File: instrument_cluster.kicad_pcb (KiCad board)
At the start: 2 copper layers, 146 x 45.7 mm, 76 parts, among them J1 Conn_02x16_Top_Bottom, J2 Conn_02x16_Top_Bottom, J3 USB mini-B SMD, J4 NOT_FITTED_SWD_Conn_01x04_Male, J5 54819-0572, J6 NOT_FITTED_SWD_Conn_01x04_Male, U1 LM2575S-5.0_NOPB, U10 74HC4050D, U11 TJA1040T, U12 TJA1040T, U2 LM2575S-5.0_NOPB, U3 LD1117S33TR_SOT223, U4 LD1117S33TR_SOT223, U5 STM32F105RBTx, U6 TJA1040T, U7 TJA1040T, U8 74HC4050D, U9 STM32F105RBTx, Y1 Crystal KX-13 25MHz, Y2 Crystal KX-13 25MHz

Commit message: rescue the stm32 mcu_s, add pcb list info
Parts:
- moved U5 93.4 mm to (149.9, 140.9)
- moved U9 93.1 mm to (134.0, 140.9)
- moved J5 86.7 mm to (106.4, 130.2), turned to 90 degrees
- moved J3 77.6 mm to (98.5, 85.7), turned to 270 degrees
- moved J2 69.4 mm to (69.8, 88.9)
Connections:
- J1 pad 10: Net-(J1-Pad10) -> (no net)
- J1 pad 11: Net-(J1-Pad11) -> (no net)
- J1 pad 14: Net-(J1-Pad14) -> (no net)
- J1 pad 20: /RR_FOG -> (no net)
- J1 pad 23: Net-(J1-Pad23) -> (no net)
- J1 pad 24: /FR_FOG -> (no net)
- J1 pad 25: Net-(J1-Pad25) -> (no net)
- J1 pad 26: Net-(J1-Pad26) -> (no net)
- J1 pad 28: Net-(J1-Pad28) -> (no net)
- J1 pad 29: Net-(J1-Pad29) -> (no net)
- J1 pad 30: Net-(J1-Pad30) -> (no net)
- J2 pad 10: Net-(J2-Pad10) -> (no net)
- J2 pad 11: Net-(J2-Pad11) -> (no net)
- J2 pad 13: Net-(J2-Pad13) -> (no net)
- J2 pad 14: Net-(J2-Pad14) -> (no net)
- J2 pad 16: Net-(J2-Pad16) -> (no net)
- J2 pad 17: Net-(J2-Pad17) -> (no net)
- J2 pad 18: Net-(J2-Pad18) -> (no net)
- J2 pad 19: Net-(J2-Pad19) -> (no net)
- J2 pad 2: Net-(J2-Pad2) -> (no net)
- J2 pad 20: Net-(J2-Pad20) -> (no net)
- J2 pad 22: Net-(J2-Pad22) -> (no net)
- J2 pad 24: Net-(J2-Pad24) -> (no net)
- J2 pad 25: Net-(J2-Pad25) -> (no net)
- J2 pad 26: Net-(J2-Pad26) -> (no net)
- J2 pad 27: Net-(J2-Pad27) -> (no net)
- J2 pad 28: /LIN_(contact_spiral) -> (no net)
- J2 pad 29: Net-(J2-Pad29) -> (no net)
- J2 pad 3: Net-(J2-Pad3) -> (no net)
- J2 pad 30: Net-(J2-Pad30) -> (no net)
- J2 pad 31: /ESCL -> (no net)
- J2 pad 32: Net-(J2-Pad32) -> (no net)
- J2 pad 4: Net-(J2-Pad4) -> (no net)
- J2 pad 6: Net-(J2-Pad6) -> (no net)
- J2 pad 8: Net-(J2-Pad8) -> (no net)
- J3 pad 4: Net-(J3-Pad4) -> (no net)
- J5 pad 4: Net-(J5-Pad4) -> (no net)
- U10 pad 13: Net-(U10-Pad13) -> (no net)
- U10 pad 14: Net-(U10-Pad14) -> (no net)
- U10 pad 15: Net-(U10-Pad15) -> (no net)
- U10 pad 16: Net-(U10-Pad16) -> (no net)
- U5 pad 10: Net-(U5-Pad10) -> (no net)
- U5 pad 11: Net-(U5-Pad11) -> (no net)
- U5 pad 14: Net-(U5-Pad14) -> (no net)
- U5 pad 15: Net-(U5-Pad15) -> (no net)
- U5 pad 16: Net-(U5-Pad16) -> (no net)
- U5 pad 17: Net-(U5-Pad17) -> (no net)
- U5 pad 2: Net-(U5-Pad2) -> (no net)
- U5 pad 20: Net-(U5-Pad20) -> (no net)
- U5 pad 21: Net-(U5-Pad21) -> (no net)
- U5 pad 22: Net-(U5-Pad22) -> (no net)
- U5 pad 23: Net-(U5-Pad23) -> (no net)
- U5 pad 24: Net-(U5-Pad24) -> (no net)
- U5 pad 25: Net-(U5-Pad25) -> (no net)
- U5 pad 26: Net-(U5-Pad26) -> (no net)
- U5 pad 27: Net-(U5-Pad27) -> (no net)
- U5 pad 28: Net-(U5-Pad28) -> (no net)
- U5 pad 29: Net-(U5-Pad29) -> (no net)
- U5 pad 3: Net-(U5-Pad3) -> (no net)
- U5 pad 30: Net-(U5-Pad30) -> (no net)
- U5 pad 33: Net-(U5-Pad33) -> (no net)
- U5 pad 34: Net-(U5-Pad34) -> (no net)
- U5 pad 35: Net-(U5-Pad35) -> (no net)
- U5 pad 36: Net-(U5-Pad36) -> (no net)
- U5 pad 37: Net-(U5-Pad37) -> (no net)
- U5 pad 38: Net-(U5-Pad38) -> (no net)
- U5 pad 39: Net-(U5-Pad39) -> (no net)
- U5 pad 4: Net-(U5-Pad4) -> (no net)
- U5 pad 40: Net-(U5-Pad40) -> (no net)
- U5 pad 41: Net-(U5-Pad41) -> (no net)
- U5 pad 43: Net-(U5-Pad43) -> (no net)
- U5 pad 50: Net-(U5-Pad50) -> (no net)
- U5 pad 51: Net-(U5-Pad51) -> (no net)
- U5 pad 52: Net-(U5-Pad52) -> (no net)
- U5 pad 53: Net-(U5-Pad53) -> (no net)
- U5 pad 54: Net-(U5-Pad54) -> (no net)
- U5 pad 55: Net-(U5-Pad55) -> (no net)
- U5 pad 56: Net-(U5-Pad56) -> (no net)
- U5 pad 59: Net-(U5-Pad59) -> (no net)
- U5 pad 60: Net-(U5-Pad60) -> (no net)
- U5 pad 7: Net-(U5-Pad7) -> (no net)
- U5 pad 8: Net-(U5-Pad8) -> (no net)
- U5 pad 9: Net-(U5-Pad9) -> (no net)
- U8 pad 13: Net-(U8-Pad13) -> (no net)
- U8 pad 14: Net-(U8-Pad14) -> (no net)
- U8 pad 15: Net-(U8-Pad15) -> (no net)
- U8 pad 16: Net-(U8-Pad16) -> (no net)
- U9 pad 10: Net-(U9-Pad10) -> (no net)
- U9 pad 14: Net-(U9-Pad14) -> (no net)
- U9 pad 16: Net-(U9-Pad16) -> (no net)
- U9 pad 2: Net-(U9-Pad2) -> (no net)
- U9 pad 20: Net-(U9-Pad20) -> (no net)
- U9 pad 25: Net-(U9-Pad25) -> (no net)
- U9 pad 26: Net-(U9-Pad26) -> (no net)
- U9 pad 27: Net-(U9-Pad27) -> (no net)
- U9 pad 28: Net-(U9-Pad28) -> (no net)
- U9 pad 29: /Module B (2can_filter+extra)/LIN_TXD -> (no net)
- U9 pad 3: Net-(U9-Pad3) -> (no net)
- U9 pad 30: /Module B (2can_filter+extra)/LIN_RXD -> (no net)
- U9 pad 33: /Module B (2can_filter+extra)/LIN_SLP -> (no net)
- U9 pad 34: Net-(U9-Pad34) -> (no net)
- U9 pad 35: Net-(U9-Pad35) -> (no net)
- U9 pad 36: Net-(U9-Pad36) -> (no net)
- U9 pad 4: Net-(U9-Pad4) -> (no net)
- U9 pad 41: Net-(U9-Pad41) -> (no net)
- U9 pad 43: Net-(U9-Pad43) -> (no net)
- U9 pad 50: Net-(U9-Pad50) -> (no net)
- U9 pad 51: Net-(U9-Pad51) -> (no net)
- U9 pad 53: Net-(U9-Pad53) -> (no net)
- U9 pad 54: Net-(U9-Pad54) -> (no net)
- U9 pad 55: Net-(U9-Pad55) -> (no net)
- U9 pad 56: Net-(U9-Pad56) -> (no net)
- U9 pad 59: Net-(U9-Pad59) -> (no net)
- U9 pad 60: Net-(U9-Pad60) -> (no net)
- U9 pad 7: Net-(U9-Pad7) -> (no net)
- U9 pad 8: Net-(U9-Pad8) -> (no net)
- U9 pad 9: Net-(U9-Pad9) -> (no net)

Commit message: pcb part replace
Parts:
- U2: footprint zulljon:TO170P1435X457-6N -> TO_SOT_Packages_SMD:TO-263-5_TabPin6
- U5, U9: moved to B.Cu
- moved D2 93.2 mm to (191.5, 126.0), turned to 270 degrees
- moved C2 89.3 mm to (186.0, 124.8), turned to 270 degrees
- moved U2 80.3 mm to (173.8, 121.1)
- moved D4 78.5 mm to (140.5, 126.5), turned to 270 degrees
- moved U3 78.0 mm to (132.0, 125.5)
- moved L2 77.1 mm to (158.0, 123.0), turned to 270 degrees
- moved C4 76.8 mm to (147.0, 124.5), turned to 90 degrees
- moved D1 65.7 mm to (191.5, 89.5), turned to 270 degrees
- moved C1 62.5 mm to (186.0, 90.8), turned to 270 degrees
- moved U1 56.6 mm to (173.5, 94.0)
- moved D5 51.1 mm to (148.0, 98.5)
- moved L1 48.2 mm to (158.0, 93.0), turned to 270 degrees
- moved U9 45.5 mm to (102.3, 108.2)
- moved C3 44.0 mm to (146.5, 91.5), turned to 90 degrees
- moved U5 36.9 mm to (131.8, 108.8)
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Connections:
- C3 pad 1: /+5V_B -> /power_supply/+5V_B_module
- C4 pad 1: /+5V_A -> /power_supply/+5V_A_module
- D3 pad 2: /+5V_B -> /power_supply/+5V_B_module
- D4 pad 2: /+5V_A -> /power_supply/+5V_A_module
- L1 pad 2: /+5V_B -> /power_supply/+5V_B_module
- L2 pad 2: /+5V_A -> /power_supply/+5V_A_module
- U1 pad 4: /+5V_B -> /power_supply/+5V_B_module
- U2 pad 4: /+5V_A -> /power_supply/+5V_A_module

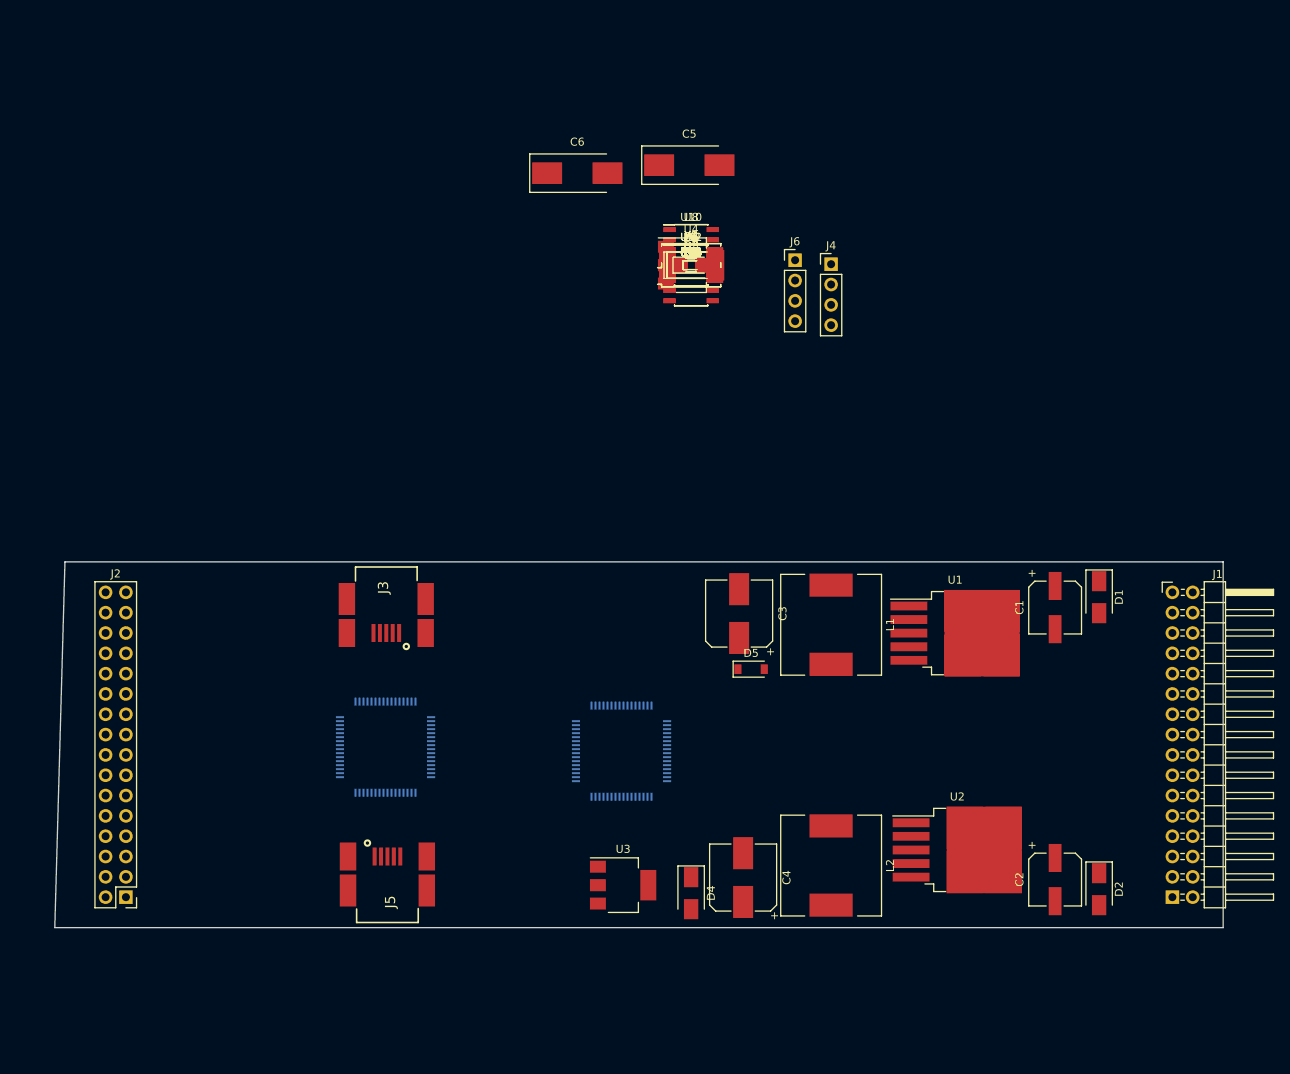
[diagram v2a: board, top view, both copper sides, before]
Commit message: fix margins, circuit to edge more >=0.3 mm
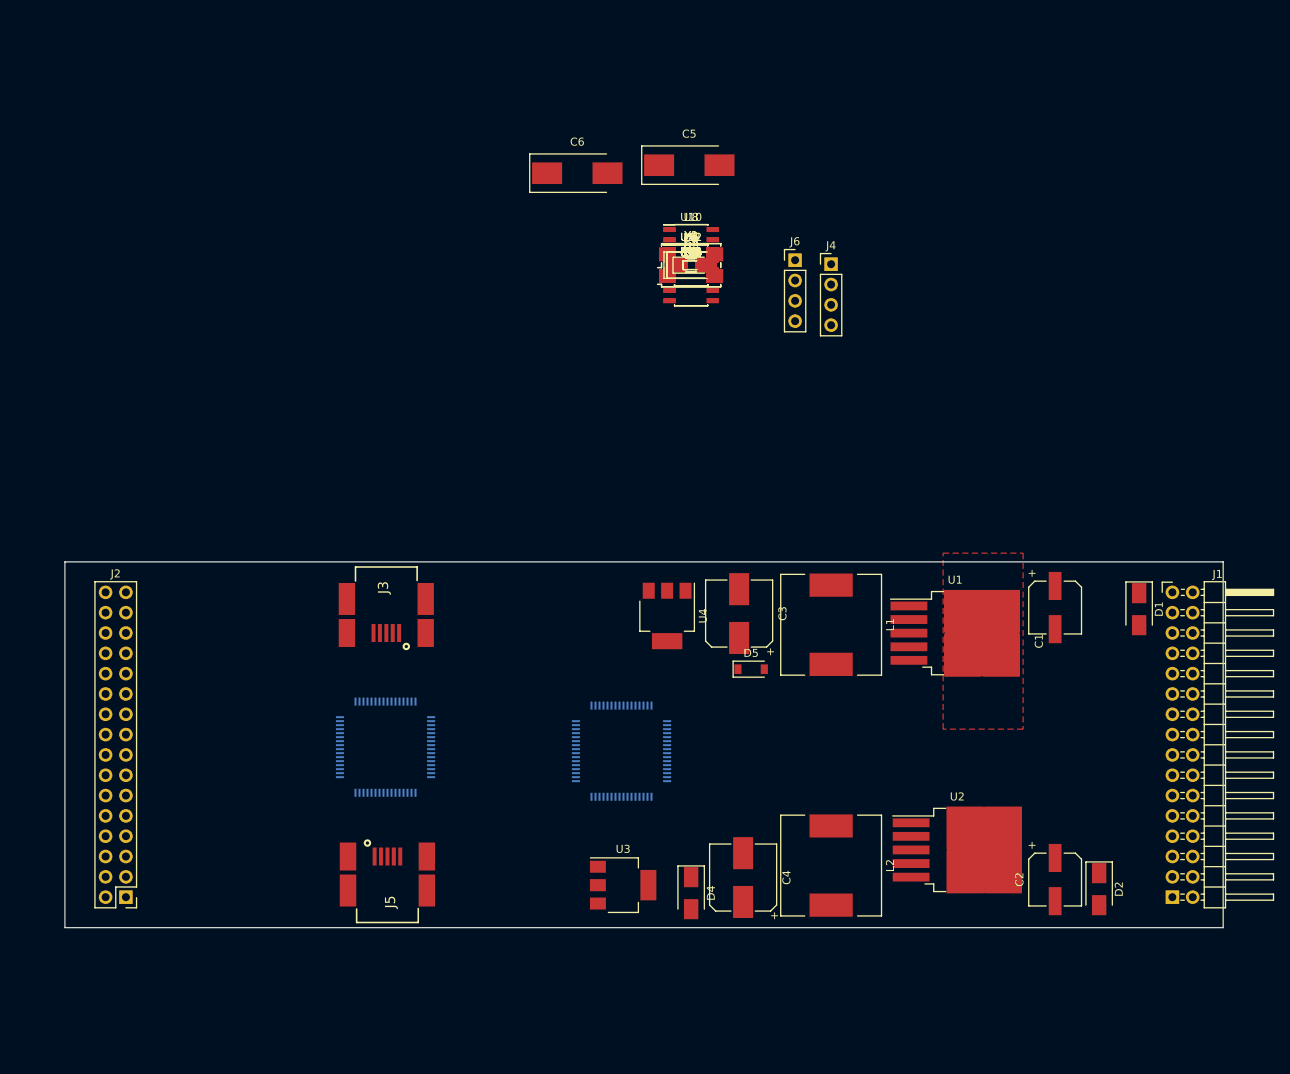
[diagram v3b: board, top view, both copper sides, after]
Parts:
- moved U4 43.9 mm to (137.5, 91.8), turned to 270 degrees
- moved D1 5.22 mm to (196.5, 91.0)
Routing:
- added copper zone on F.Cu, net GND
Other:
- board size 146 x 45.7 mm -> 144.8 x 45.7 mm
- board text added: "edge.cuts - grid 1.27 margins - grid 0.127 trace - 0.5"
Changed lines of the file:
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@@
     (area 60.884999 85.014999 207.085001 130.885001)
     (thickness 1.6)
-    (drawings 9)
+    (drawings 12)
     (tracks 0)
     (zones 0)
@@
     (40 Dwgs.User user)
     (41 Cmts.User user)
-    (42 Eco1.User user hide)
+    (42 Eco1.User user)
     (43 Eco2.User user hide)
     (44 Edge.Cuts user)
@@
     (last_trace_width 0.25)
     (trace_clearance 0.2)
-    (zone_clearance 0.508)
-    (zone_45_only no)
+    (zone_clearance 0.3)
+    (zone_45_only yes)
     (trace_min 0.2)
     (segment_width 0.2)
@@
     (descr "SMT capacitor, aluminium electrolytic, 6.3x7.7")
     (attr smd)
-    (fp_text reference C1 (at 0 4.43 270) (layer F.SilkS)
+    (fp_text reference C1 (at 4.2 2 270) (layer F.SilkS)
       (effects (font (size 1 1) (thickness 0.15)))
     )
@@
   )
   (module Diodes_SMD:D_SMA (layer F.Cu)
-    (at 191.5 89.5 270)
+    (at 196.5 91 270)
     (descr "Diode SMA (DO-214AC)")
     (tags "Diode SMA (DO-214AC)")
@@
   )
   (module TO_SOT_Packages_SMD:SOT-223-3_TabPin2 (layer F.Cu)
-    (at 140.5011 48.0036)
+    (at 137.5 91.85 270)
     (descr "module CMS SOT223 4 pins")
     (tags "CMS SOT")
     (attr smd)
-    (fp_text reference U4 (at 0 -4.5) (layer F.SilkS)
+    (fp_text reference U4 (at 0 -4.5 270) (layer F.SilkS)
       (effects (font (size 1 1) (thickness 0.15)))
     )
-    (fp_text value LD1117S33TR_SOT223 (at 0 4.5) (layer F.Fab)
+    (fp_text value LD1117S33TR_SOT223 (at 0 4.5 270) (layer F.Fab)
       (effects (font (size 1 1) (thickness 0.15)))
     )
-    (fp_text user %R (at 0 0 90) (layer F.Fab)
+    (fp_text user %R (at 0 0 360) (layer F.Fab)
       (effects (font (size 0.8 0.8) (thickness 0.12)))
     )
@@
     (fp_line (start -1.85 3.35) (end 1.85 3.35) (layer F.Fab) (width 0.1))
     (fp_line (start 1.85 -3.35) (end 1.85 3.35) (layer F.Fab) (width 0.1))
-    (pad 2 smd rect (at 3.15 0) (size 2 3.8) (layers F.Cu F.Paste F.Mask)
+    (pad 2 smd rect (at 3.15 0 270) (size 2 3.8) (layers F.Cu F.Paste F.Mask)
       (net 7 /+3V3_B))
-    (pad 2 smd rect (at -3.15 0) (size 2 1.5) (layers F.Cu F.Paste F.Mask)
+    (pad 2 smd rect (at -3.15 0 270) (size 2 1.5) (layers F.Cu F.Paste F.Mask)
       (net 7 /+3V3_B))
-    (pad 3 smd rect (at -3.15 2.3) (size 2 1.5) (layers F.Cu F.Paste F.Mask)
+    (pad 3 smd rect (at -3.15 2.3 270) (size 2 1.5) (layers F.Cu F.Paste F.Mask)
       (net 4 /+5V_B))
-    (pad 1 smd rect (at -3.15 -2.3) (size 2 1.5) (layers F.Cu F.Paste F.Mask)
+    (pad 1 smd rect (at -3.15 -2.3 270) (size 2 1.5) (layers F.Cu F.Paste F.Mask)
       (net 2 GND))
     (model ${KISYS3DMOD}/TO_SOT_Packages_SMD.3dshapes/SOT-223.wrl
@@
     )
   )
-  (gr_line (start 62.23 85.09) (end 207.01 85.09) (layer Margin) (width 0.2))
-  (gr_line (start 60.96 130.81) (end 62.23 85.09) (layer Margin) (width 0.2))
-  (gr_line (start 207.01 130.81) (end 60.96 130.81) (layer Margin) (width 0.2))
-  (gr_line (start 207.01 85.09) (end 207.01 130.81) (layer Margin) (width 0.2))
-  (gr_line (start 60.96 130.81) (end 62.23 85.09) (layer Edge.Cuts) (width 0.15))
-  (gr_line (start 207.01 130.81) (end 60.96 130.81) (layer Edge.Cuts) (width 0.15))
+  (dimension 144.78 (width 0.3) (layer Eco1.User)
+    (gr_text "144,780 мм" (at 134.62 148.924) (layer Eco1.User)
+      (effects (font (size 1.5 1.5) (thickness 0.3)))
+    )
+    (feature1 (pts (xy 62.23 85.09) (xy 62.23 150.274)))
+    (feature2 (pts (xy 207.01 85.09) (xy 207.01 150.274)))
+    (crossbar (pts (xy 207.01 147.574) (xy 62.23 147.574)))
+    (arrow1a (pts (xy 62.23 147.574) (xy 63.356504 146.987579)))
+    (arrow1b (pts (xy 62.23 147.574) (xy 63.356504 148.160421)))
+    (arrow2a (pts (xy 207.01 147.574) (xy 205.883496 146.987579)))
+    (arrow2b (pts (xy 207.01 147.574) (xy 205.883496 148.160421)))
+  )
+  (dimension 0.381 (width 0.3) (layer Eco1.User)
+    (gr_text "0,381 мм" (at 219.536 85.2805 270) (layer Eco1.User)
+      (effects (font (size 1.5 1.5) (thickness 0.3)))
+    )
+    (feature1 (pts (xy 207.01 85.471) (xy 220.886 85.471)))
+    (feature2 (pts (xy 207.01 85.09) (xy 220.886 85.09)))
+    (crossbar (pts (xy 218.186 85.09) (xy 218.186 85.471)))
+    (arrow1a (pts (xy 218.186 85.471) (xy 217.599579 84.344496)))
+    (arrow1b (pts (xy 218.186 85.471) (xy 218.772421 84.344496)))
+    (arrow2a (pts (xy 218.186 85.09) (xy 217.599579 86.216504)))
+    (arrow2b (pts (xy 218.186 85.09) (xy 218.772421 86.216504)))
+  )
+  (gr_text "edge.cuts - grid 1.27\nmargins - grid 0.127\ntrace - 0.5" (at 264.16 93.98) (layer Eco1.User)
+    (effects (font (size 1.5 1.5) (thickness 0.3)))
+  )
+  (gr_line (start 62.611 85.471) (end 206.629 85.471) (layer Margin) (width 0.2))
+  (gr_line (start 62.611 130.429) (end 62.611 85.471) (layer Margin) (width 0.2))
+  (gr_line (start 206.629 130.429) (end 62.611 130.429) (layer Margin) (width 0.2))
+  (gr_line (start 206.629 85.471) (end 206.629 130.429) (layer Margin) (width 0.2))
+  (gr_line (start 62.23 130.81) (end 62.23 85.09) (layer Edge.Cuts) (width 0.15))
+  (gr_line (start 207.01 130.81) (end 62.23 130.81) (layer Edge.Cuts) (width 0.15))
   (gr_line (start 207.01 85.09) (end 62.23 85.09) (layer Edge.Cuts) (width 0.15))
   (gr_line (start 207.01 130.81) (end 207.01 85.09) (layer Edge.Cuts) (width 0.15))
@@
     (arrow2b (pts (xy 223.259218 130.81) (xy 222.672797 129.683496)))
   )
+  (zone (net 2) (net_name GND) (layer F.Cu) (hatch none 0.508)
+    (priority 1)
+    (connect_pads thru_hole_only (clearance 0.3))
+    (min_thickness 0.0254)
+    (fill yes (mode segment) (arc_segments 32) (thermal_gap 0.508) (thermal_bridge_width 0.508) (smoothing chamfer) (radius 2))
+    (polygon
+      (pts
+        (xy 182 84) (xy 182 106) (xy 172 106) (xy 172 84)
+      )
+    )
+  )
 )

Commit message: setup design rule
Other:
- net class +12V added: clearance 0.3, trace_width 0.6, via_dia 0.6, via_drill 0.3
- net class +3V3 added: clearance 0.3, trace_width 0.3, via_dia 0.5, via_drill 0.3
- net class +5V added: clearance 0.3, trace_width 0.3, via_dia 0.5, via_drill 0.3
- net class Default: trace_width 0.25 -> 0.2; via_dia 0.6 -> 0.5; via_drill 0.4 -> 0.3
- net class GND added: clearance 0.3, trace_width 0.4, via_dia 0.6, via_drill 0.3
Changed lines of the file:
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@@
   )
   (setup
-    (last_trace_width 0.25)
+    (last_trace_width 0.2)
     (trace_clearance 0.2)
     (zone_clearance 0.3)
@@
     (segment_width 0.2)
     (edge_width 0.15)
-    (via_size 0.6)
-    (via_drill 0.4)
+    (via_size 0.5)
+    (via_drill 0.3)
     (via_min_size 0.4)
     (via_min_drill 0.3)
-    (uvia_size 0.3)
-    (uvia_drill 0.1)
+    (uvia_size 0.35)
+    (uvia_drill 0.2)
     (uvias_allowed no)
     (uvia_min_size 0.2)
@@
   (net_class Default "Это класс цепей по умолчанию."
     (clearance 0.2)
-    (trace_width 0.25)
-    (via_dia 0.6)
-    (via_drill 0.4)
-    (uvia_dia 0.3)
-    (uvia_drill 0.1)
-    (add_net /+3V3_A)
-    (add_net /+3V3_B)
-    (add_net /+5V_A)
-    (add_net /+5V_B)
+    (trace_width 0.2)
+    (via_dia 0.5)
+    (via_drill 0.3)
+    (uvia_dia 0.35)
+    (uvia_drill 0.2)
     (add_net /ANTI-THEFT)
     (add_net /BELT_MINDER)
     (add_net "/BRAKE(fluid_level)")
     (add_net "/ENGINE(coolant_level)")
-    (add_net /FUEL_TANK_in)
     (add_net /FUEL_TANK_out1)
     (add_net /FUEL_TANK_out2)
@@
     (add_net /MS_CAN_H)
     (add_net /MS_CAN_L)
-    (add_net "/Module A (2can_filter)/USB_D+")
-    (add_net "/Module A (2can_filter)/USB_D-")
     (add_net "/Module B (2can_filter+extra)/CAN1_RX")
     (add_net "/Module B (2can_filter+extra)/CAN1_TX")
     (add_net "/Module B (2can_filter+extra)/CAN2_RX")
     (add_net "/Module B (2can_filter+extra)/CAN2_TX")
-    (add_net "/Module B (2can_filter+extra)/USB_D+")
-    (add_net "/Module B (2can_filter+extra)/USB_D-")
     (add_net "/Module B (2can_filter+extra)/belt")
     (add_net "/Module B (2can_filter+extra)/brake_fluid_level")
@@
     (add_net /PARKING_BRAKE)
     (add_net /TRIP_COMPUTER)
-    (add_net /VBATT)
-    (add_net /power_supply/+12V_A)
-    (add_net /power_supply/+5V_A_module)
-    (add_net /power_supply/+5V_B_module)
-    (add_net GND)
     (add_net "Net-(C21-Pad1)")
     (add_net "Net-(C22-Pad1)")
@@
     (add_net "Net-(U5-Pad62)")
   )
+  (net_class +12V ""
+    (clearance 0.3)
+    (trace_width 0.6)
+    (via_dia 0.6)
+    (via_drill 0.3)
+    (uvia_dia 0.35)
+    (uvia_drill 0.2)
+    (add_net /FUEL_TANK_in)
+    (add_net /VBATT)
+    (add_net /power_supply/+12V_A)
+  )
+  (net_class +3V3 ""
+    (clearance 0.3)
+    (trace_width 0.3)
+    (via_dia 0.5)
+    (via_drill 0.3)
+    (uvia_dia 0.35)
+    (uvia_drill 0.2)
+    (add_net /+3V3_A)
+    (add_net /+3V3_B)
+  )
+  (net_class +5V ""
+    (clearance 0.3)
+    (trace_width 0.3)
+    (via_dia 0.5)
+    (via_drill 0.3)
+    (uvia_dia 0.35)
+    (uvia_drill 0.2)
+    (add_net /+5V_A)
+    (add_net /+5V_B)
+    (add_net "/Module A (2can_filter)/USB_D+")
+    (add_net "/Module A (2can_filter)/USB_D-")
+    (add_net "/Module B (2can_filter+extra)/USB_D+")
+    (add_net "/Module B (2can_filter+extra)/USB_D-")
+    (add_net /power_supply/+5V_A_module)
+    (add_net /power_supply/+5V_B_module)
+  )
+  (net_class GND ""
+    (clearance 0.3)
+    (trace_width 0.4)
+    (via_dia 0.6)
+    (via_drill 0.3)
+    (uvia_dia 0.35)
+    (uvia_drill 0.2)
+    (add_net GND)
+  )
   (module Capacitors_SMD:CP_Elec_6.3x7.7 (layer F.Cu)

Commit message: setup design rule2
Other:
- rule trace_min: 0.2 -> 0.089
- rule via_min_size: 0.4 -> 0.3
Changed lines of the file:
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@@
     (zone_clearance 0.3)
     (zone_45_only yes)
-    (trace_min 0.2)
+    (trace_min 0.089)
     (segment_width 0.2)
     (edge_width 0.15)
     (via_size 0.5)
     (via_drill 0.3)
-    (via_min_size 0.4)
+    (via_min_size 0.3)
     (via_min_drill 0.3)
     (uvia_size 0.35)
